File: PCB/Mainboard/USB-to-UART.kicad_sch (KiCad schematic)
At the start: 10 parts, among them U9 CP2102N

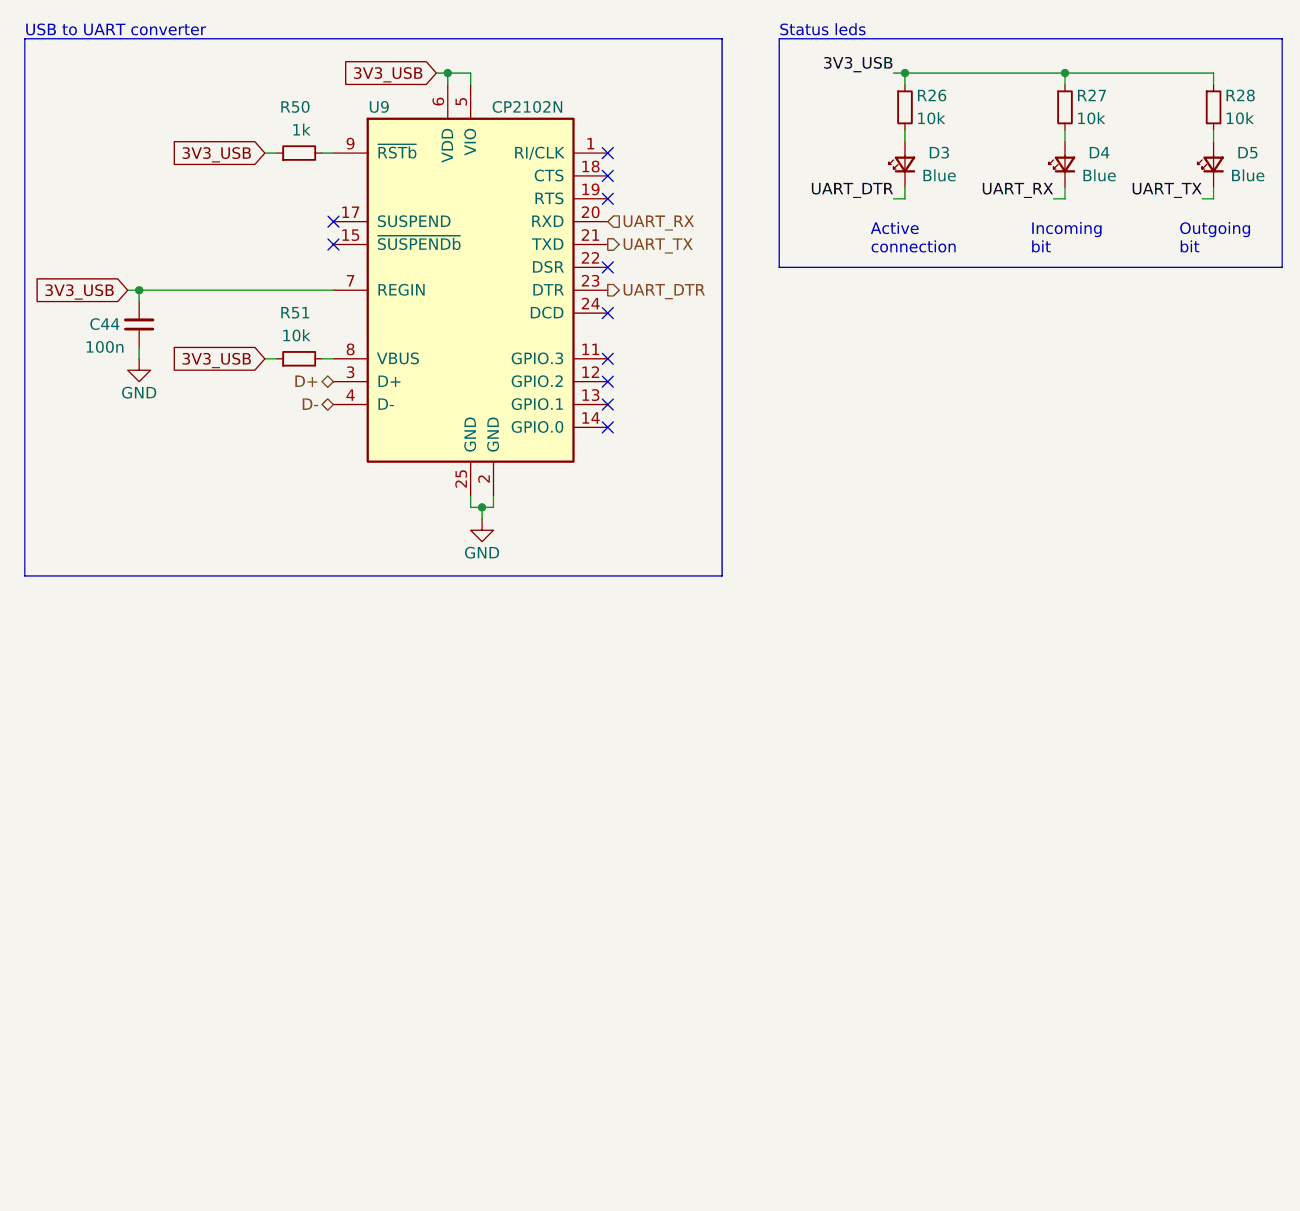
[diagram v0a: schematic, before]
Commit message: Update schematic and lay-out
- Swap out CP2102N, ATmega328PB and CP with new Kicad 6 symbol
- Correct all links to point to new zoudio_symbols and zoudio_footprint libraries
- Lay-out updated, only antenna is left to update.
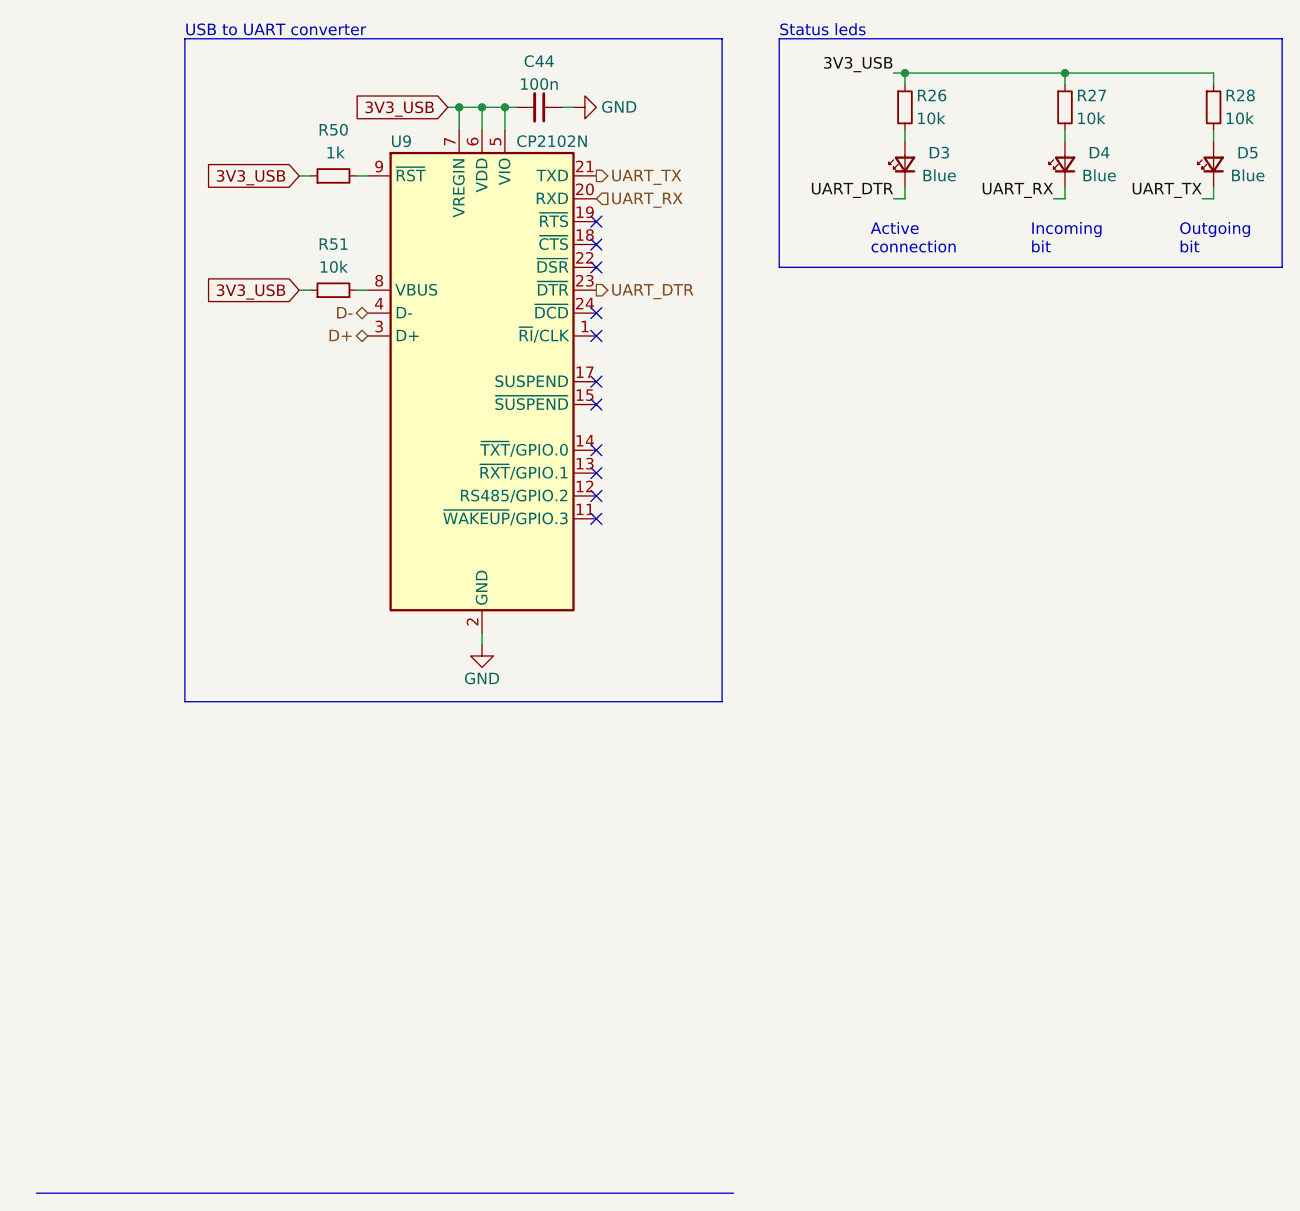
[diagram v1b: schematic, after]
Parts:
- removed U9: CP2102N, Package_DFN_QFN:QFN-24-1EP_4x4mm_P0.5mm_EP2.6x2.6mm, symbol Interface_USB:CP2102N-A01-GQFN24
- added U9: CP2102N, Package_DFN_QFN:QFN-24-1EP_4x4mm_P0.5mm_EP2.6x2.6mm, symbol Interface_USB:CP2102N-Axx-xQFN24
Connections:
- net 3V3_USB: now also U9.5 (VIO), U9.6 (VDD), U9.7 (VREGIN)
- net D+: now also U9.3 (D+)
- net D-: now also U9.4 (D-)
- net GND: now also U9.2 (GND), U9.25 (GND)
- net UART_DTR: now also U9.23 (~{DTR})
- net UART_RX: now also U9.20 (RXD)
- net UART_TX: now also U9.21 (TXD)
- net at R51.2: now also U9.8 (VBUS)
- net at R50.2: now also U9.9 (~{RST})
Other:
- moved on the sheet: C44, R50, R51
